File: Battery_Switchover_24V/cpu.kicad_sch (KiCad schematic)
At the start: 44 parts, among them J8 USB_C_Receptacle_USB2.0_14P, SW1 SW_Push, U3 LPC11U14FBD48-201, U4 AMC1300BDWV, U5 TPS54560BDDA, U6 AMS1117-3.3, Y1 12.000MHz

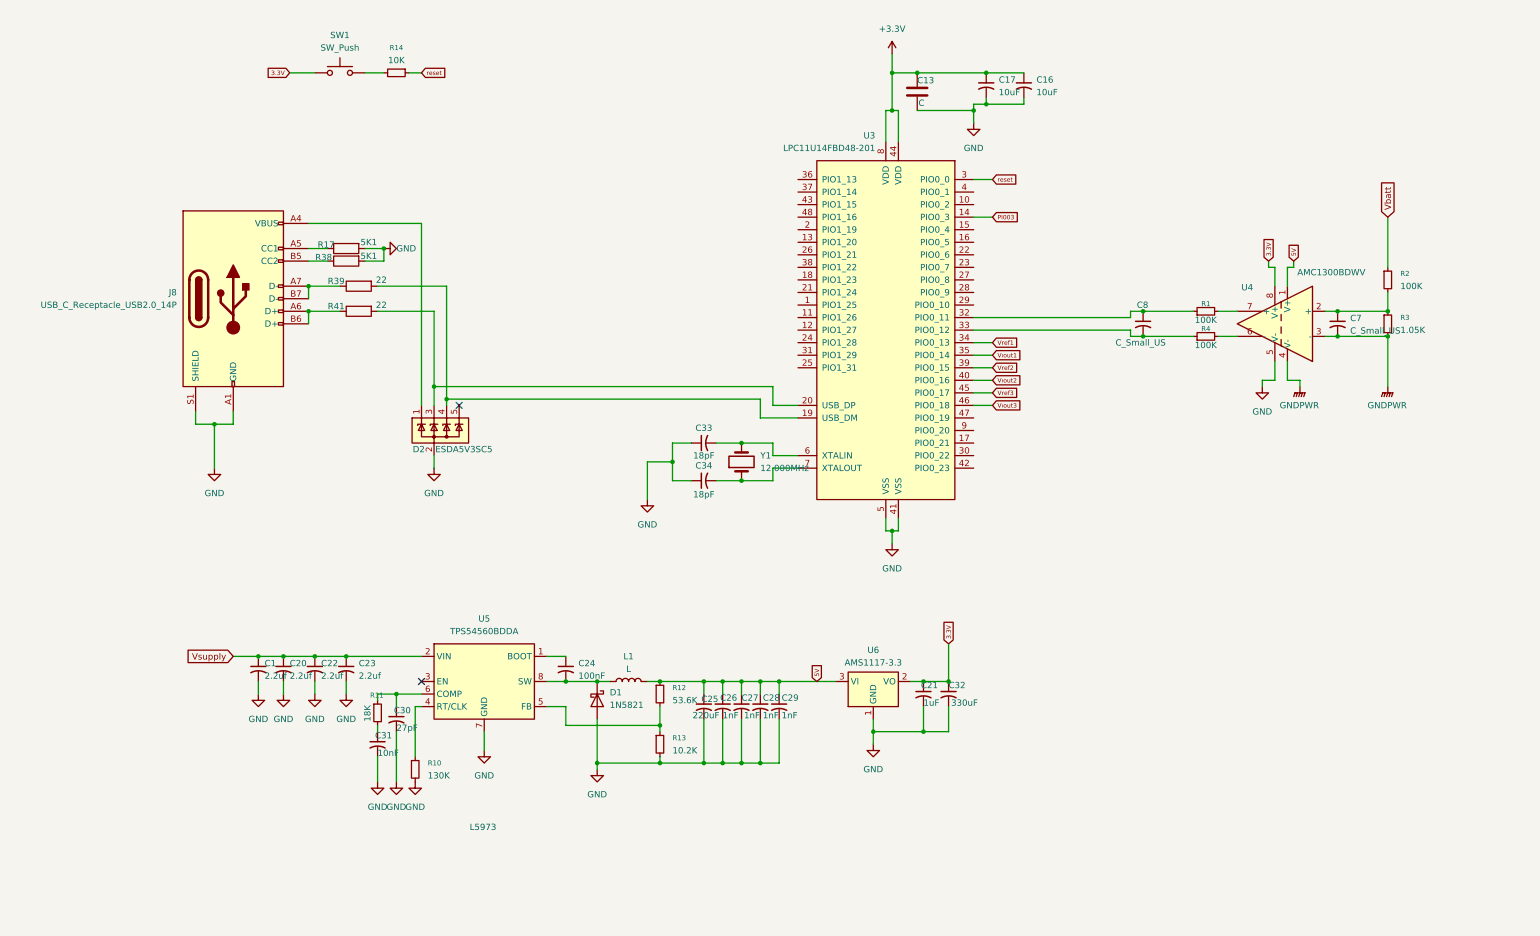
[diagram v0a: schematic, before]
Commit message: General Improvements
Mosfet sayısı 1 e düştü polarize cap ler değiştirildi voltage converter değiştirildi
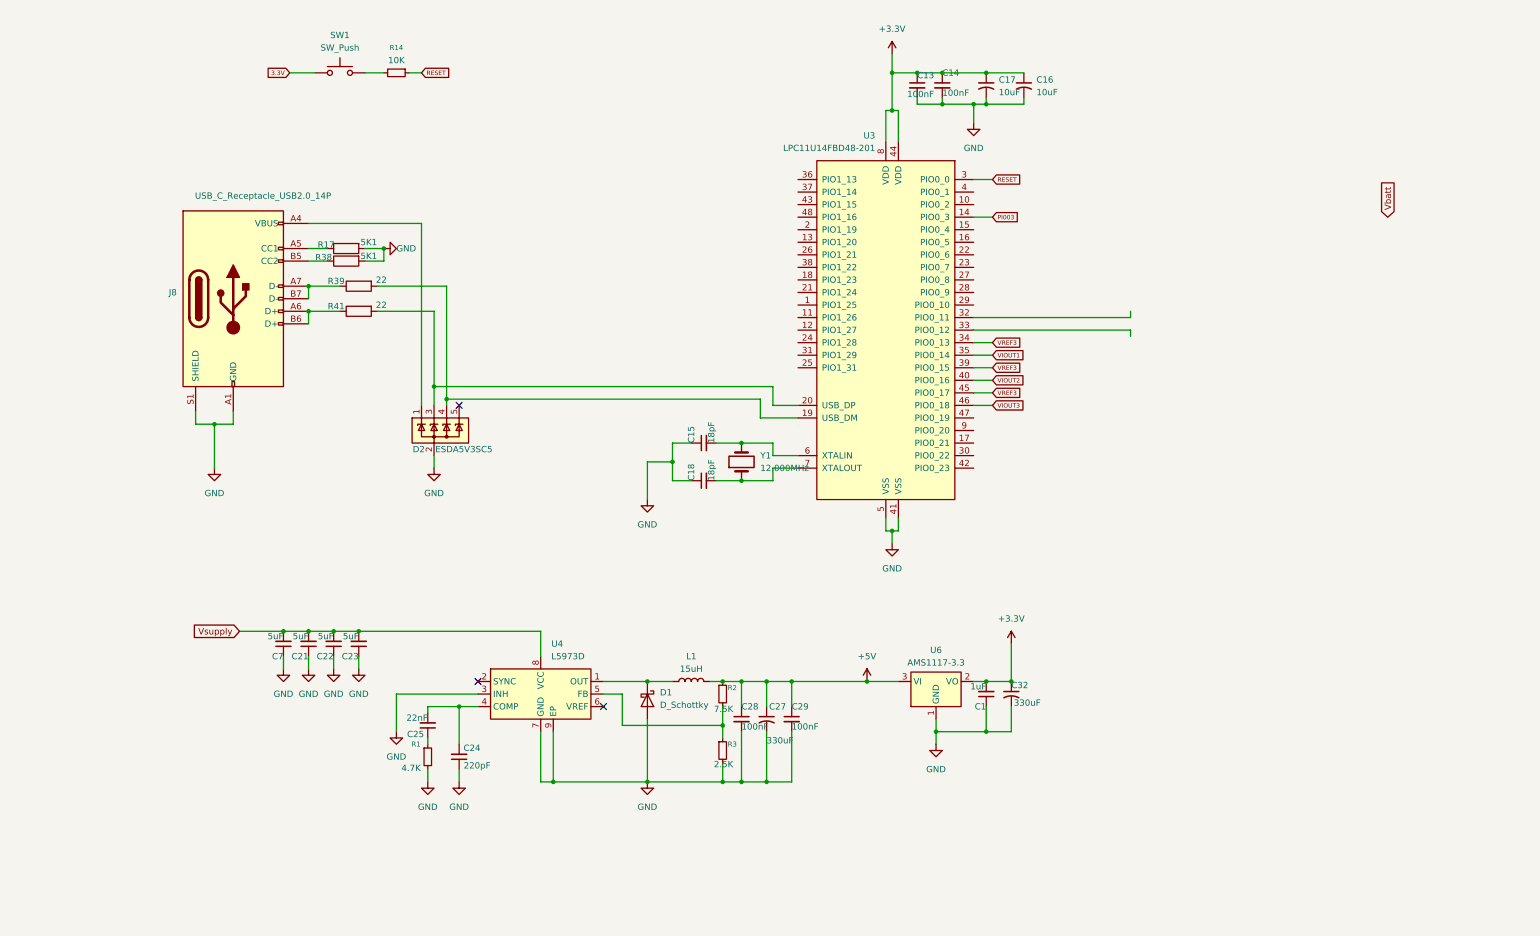
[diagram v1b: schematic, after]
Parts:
- removed C1, C20, C22, C23: 2.2uf, symbol Device:C_Small_US
- removed C13: C, symbol Device:C
- removed C21: 1uF, symbol Device:C_Small_US
- removed C24: 100nF, symbol Device:C_Small_US
- removed C25: 220uF, symbol Device:C_Small_US
- removed C26, C28, C29: 1nF, symbol Device:C_Small_US
- removed C30: 27pF, symbol Device:C_Small_US
- removed C31: 10nF, symbol Device:C_Small_US
- removed C33, C34: 18pF, symbol Device:C_Small_US
- removed C7, C8: C_Small_US, symbol Device:C_Small_US
- removed D1: 1N5821, Diode_THT:D_DO-201AD_P15.24mm_Horizontal, symbol Diode:1N5821
- removed R10: 130K, symbol Device:R_Small
- removed R11: 18K, symbol Device:R_Small
- removed R12: 53.6K, symbol Device:R_Small
- removed R13: 10.2K, symbol Device:R_Small
- removed R4: 100K, symbol Device:R_Small
- removed U4: AMC1300BDWV, Package_SO:SOIC-8_7.5x5.85mm_P1.27mm, symbol Amplifier_Difference:AMC1300BDWV
- removed U5: TPS54560BDDA, Package_SO:Texas_R-PDSO-G8_EP2.95x4.9mm_Mask2.4x3.1mm_ThermalVias, symbol Regulator_Switching:TPS54560BDDA
- added C1: 1uF, symbol Device:C_Small
- added C13, C14, C28, C29: 100nF, symbol Device:C_Small
- added C15, C18: 18pF, symbol Device:C_Small
- added C21, C22, C23, C7: 5uF, symbol Device:C_Small
- added C24: 220pF, symbol Device:C_Small
- added C25: 22nF, symbol Device:C_Small
- added D1: D_Schottky, symbol Device:D_Schottky
- added U4: L5973D, Package_SO:HSOP-8-1EP_3.9x4.9mm_P1.27mm_EP2.41x3.1mm_ThermalVias, symbol Regulator_Switching:L5973D
- C27: value 1nF -> 330uF
- L1: value L -> 15uH
- R1: value 100K -> 4.7K
- R2: value 100K -> 7.5K
- R3: value 1.05K -> 2.5K
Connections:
- net GNDPWR is gone; now on net GND: R3.2
- net Vref2 is gone; now on net VREF3: U3.39 (PIO0_15)
- net Vref3 is gone; now on net VREF3: U3.45 (PIO0_17)
- net +3.3V: now also C32.1, U6.2 (VO), C1.2, C13.1, C14.1
- net 3.3V: no longer C32.1, U6.2 (VO)
- net GND: now also R1.2, C1.1, C13.2, C14.2, C15.1, C18.1, C21.1, C22.1, C23.1, C24.1, C28.2, C29.2, C7.1, D1.2 (A), U4.3 (INH), U4.7 (GND), U4.9 (EP)
- net Vbatt: no longer R2.1
- net Vsupply: now also C21.2, C22.2, C23.2, C7.2, U4.8 (VCC)
- net at U3.32 (PIO0_11): no longer R1.1
- net at U3.7 (XTALOUT), Y1.1: now also C18.2
- net at L1.1: now also D1.1 (K), U4.1 (OUT)
- net at U3.6 (XTALIN), Y1.2: now also C15.2
- net at R2.2, R3.1: now also U4.5 (FB)
- net 5V renamed +5V
- net +5V: now also R2.1, C28.1, C29.1
- net Vref1 renamed VREF3
- net Vıout1 renamed VIOUT1
- net Vıout2 renamed VIOUT2
- net Vıout3 renamed VIOUT3
- net reset renamed RESET
- new net: C24.2, C25.2, U4.4 (COMP)
- new net: C25.1, R1.1
- no-connect marks 2 -> 3
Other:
- note removed: "L5973"
- moved on the sheet: C32, U6

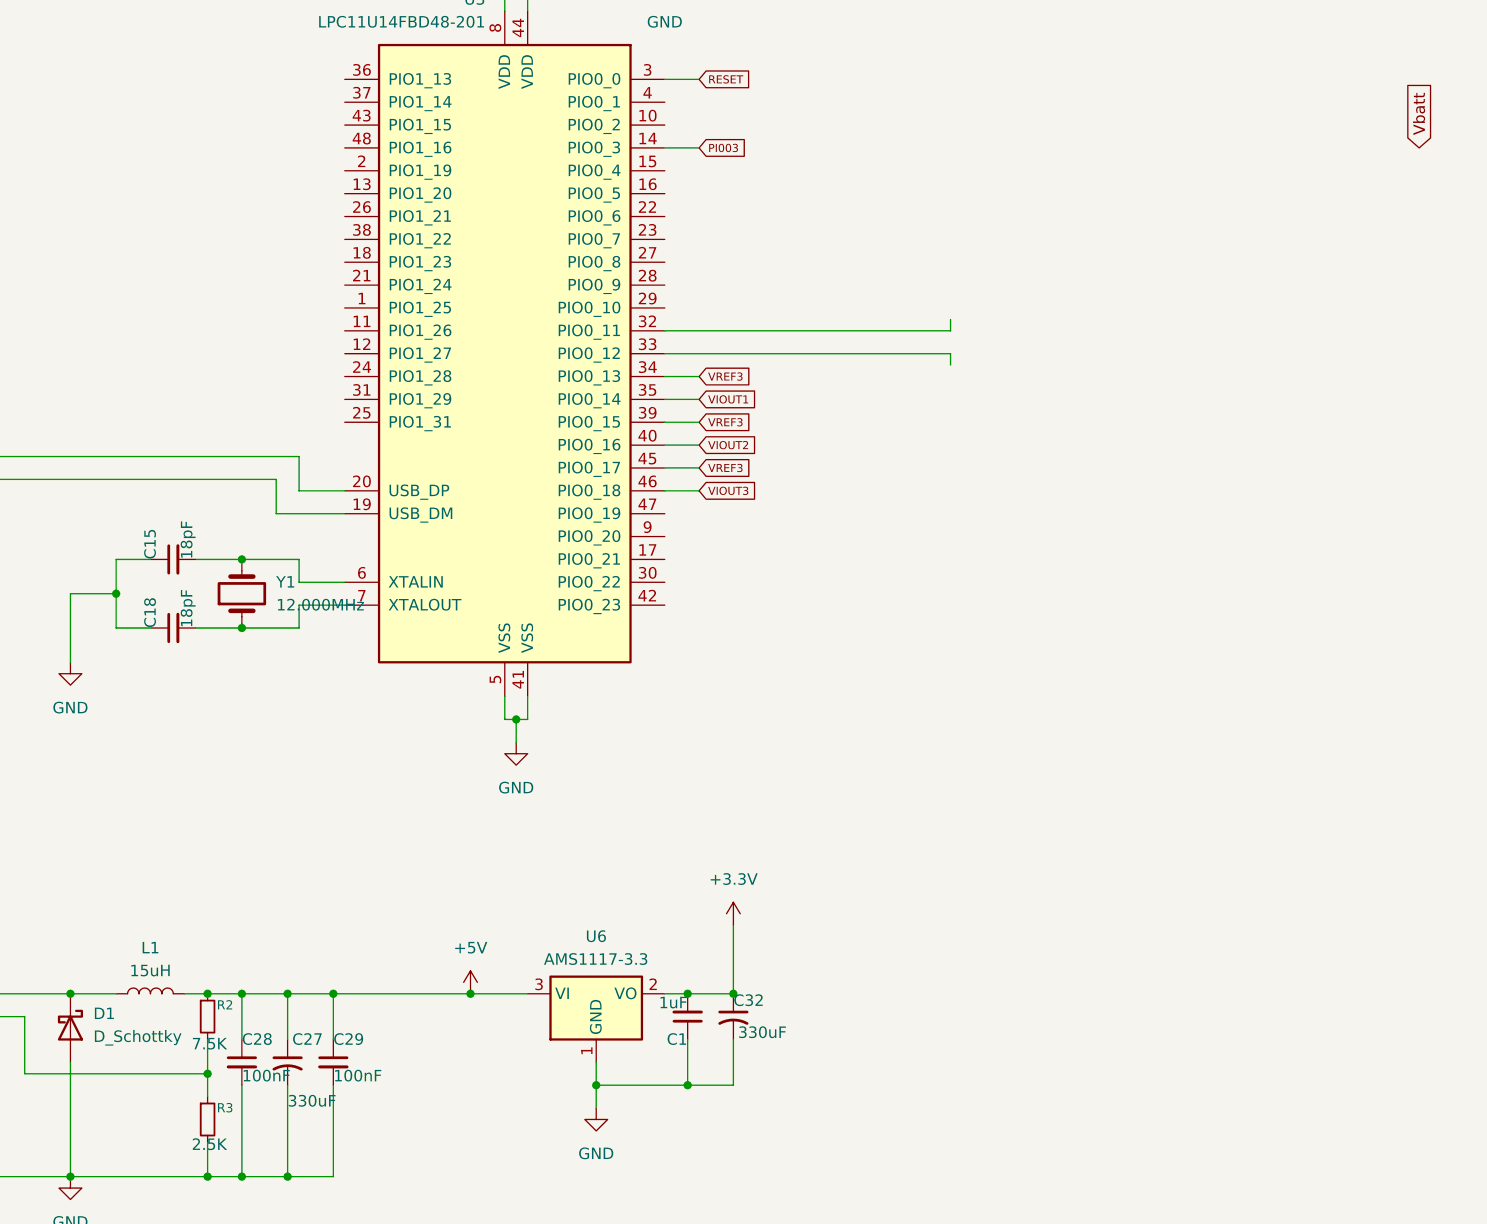
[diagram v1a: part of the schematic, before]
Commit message: Isı kontrollü eklendi bazı parçaların sembolleri değişti
Mosfetlere doğru semboller eklendi Isı kontorll IC eklendi Ledlerin bağlantıları yapıldı
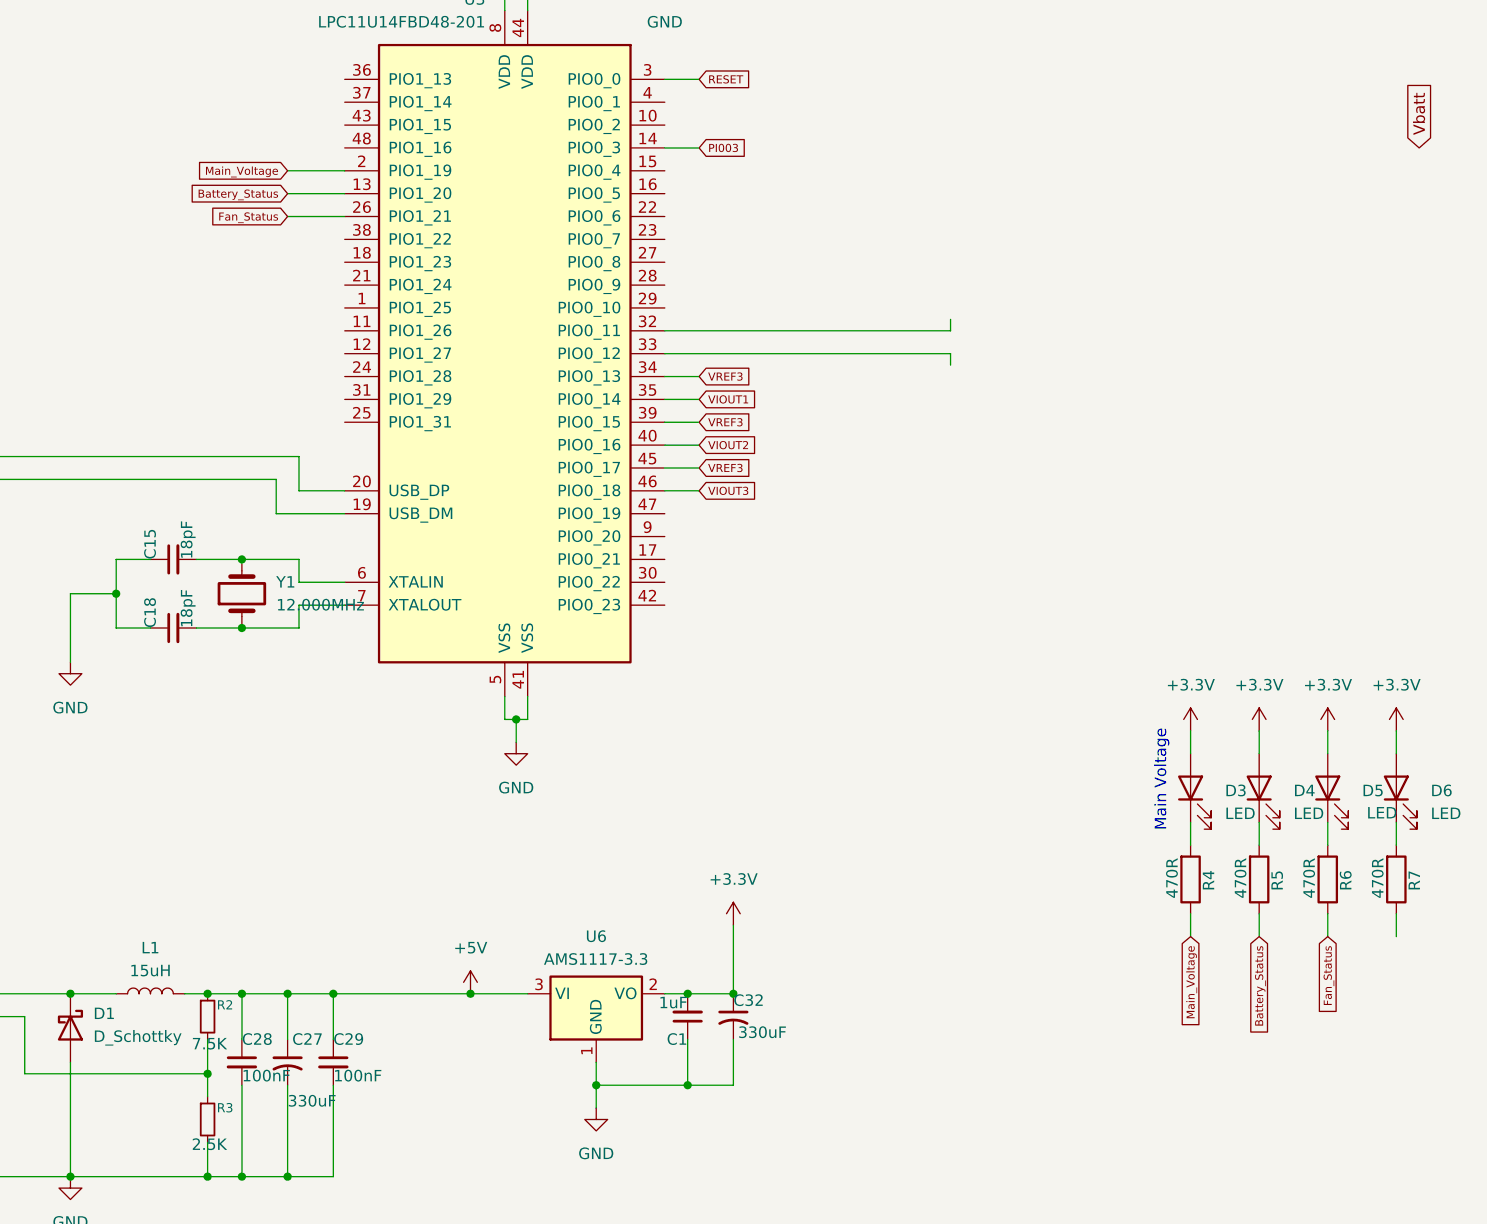
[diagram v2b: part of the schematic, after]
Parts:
- added D3, D4, D5, D6: LED, symbol Device:LED
- added R4, R5, R6, R7: 470R, Resistor_SMD:R_0603_1608Metric, symbol Device:R
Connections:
- net +3.3V: now also D3.2 (A), D4.2 (A), D5.2 (A), D6.2 (A)
- net Battery_Status: now reaches U3.13 (PIO1_20)
- net Battery_Status: now also R5.1
- net Main_Voltage: now reaches U3.2 (PIO1_19)
- net Main_Voltage: now also R4.1
- net Fan_Status: now reaches U3.26 (PIO1_21)
- net Fan_Status: now also R6.1
- new net: D5.1 (K), R6.2
- new net: D3.1 (K), R4.2
- new net: D6.1 (K), R7.2
- new net: D4.1 (K), R5.2
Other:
- note added: "Main Voltage"
